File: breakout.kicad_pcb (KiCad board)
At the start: 2 copper layers, 103 x 62 mm, 32 parts, among them CON1 SD_Card, CON2 USB-MICRO-AB, P2 CONN_01X40, P3 CONN_01X40, P4 CONN_01X40, P5 A-DF-09-A/KG-T4S, SW1 SW_PUSH

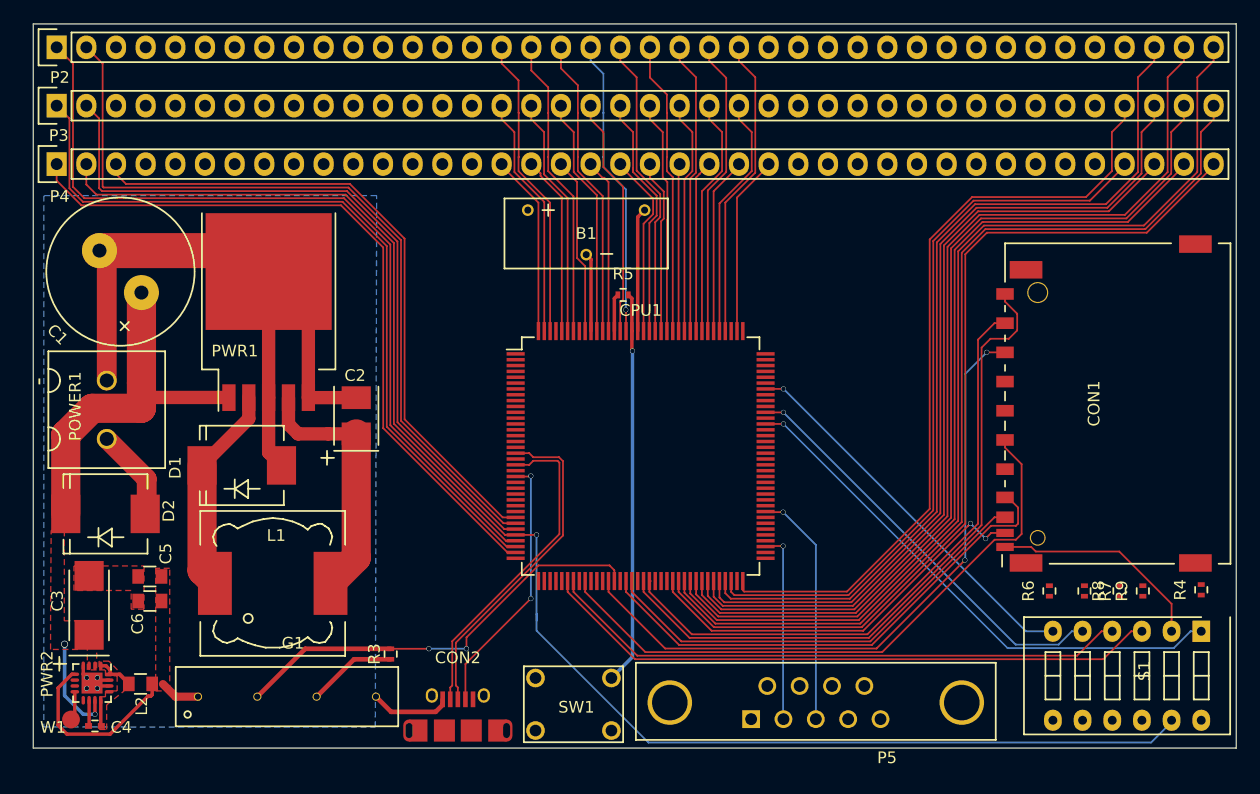
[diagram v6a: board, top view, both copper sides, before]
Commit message: routed right side of IC
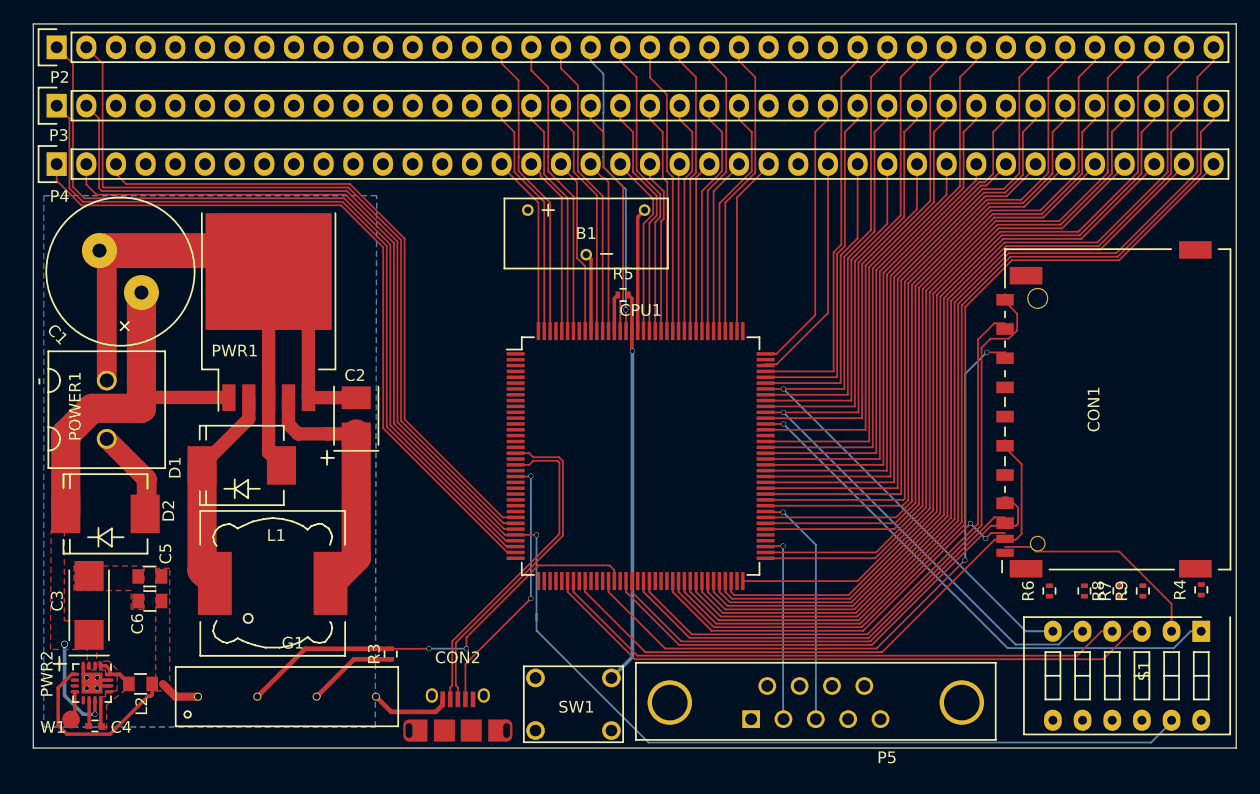
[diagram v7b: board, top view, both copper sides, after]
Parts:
- moved CON1 0.50 mm to (141.2, 146.0)
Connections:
- CPU1 pad 100: (no net) -> /P6_10
- CPU1 pad 101: (no net) -> /P6_11
- CPU1 pad 103: (no net) -> /P6_12
- CPU1 pad 104: (no net) -> /P2_10
- CPU1 pad 105: (no net) -> /P2_11
- CPU1 pad 106: (no net) -> /P2_12
- CPU1 pad 108: (no net) -> /P2_13
- CPU1 pad 73: (no net) -> /P6_0
- CPU1 pad 74: (no net) -> /P6_1
- CPU1 pad 78: (no net) -> /P6_2
- CPU1 pad 79: (no net) -> /P6_3
- CPU1 pad 80: (no net) -> /P6_4
- CPU1 pad 82: (no net) -> /P6_5
- CPU1 pad 83: (no net) -> /P6_6
- CPU1 pad 84: (no net) -> /P2_2
- CPU1 pad 85: (no net) -> /P6_7
- CPU1 pad 86: (no net) -> /P6_8
- CPU1 pad 87: (no net) -> /P2_3
- CPU1 pad 88: (no net) -> /P2_4
- CPU1 pad 89: (no net) -> /USB1_D+
- CPU1 pad 90: (no net) -> /USB1_D-
- CPU1 pad 91: (no net) -> /P2_5
- CPU1 pad 92: (no net) -> /I2C0_SCL
- CPU1 pad 93: (no net) -> /I2C0_SDA
- CPU1 pad 95: (no net) -> /P2_6
- CPU1 pad 97: (no net) -> /P6_9
- CPU1 pad 99: (no net) -> /CLK2
- P2 pad 28: (no net) -> /P2_11
- P2 pad 29: (no net) -> /P2_9
- P2 pad 30: (no net) -> /CLK2
- P2 pad 31: (no net) -> /P2_6
- P2 pad 32: (no net) -> /P2_5
- P2 pad 34: (no net) -> /P6_8
- P2 pad 35: (no net) -> /P6_6
- P2 pad 36: (no net) -> /P6_3
- P2 pad 37: (no net) -> /P6_0
- P3 pad 27: (no net) -> /P2_13
- P3 pad 28: (no net) -> /P2_10
- P3 pad 29: (no net) -> /P6_11
- P3 pad 30: (no net) -> /P2_8
- P3 pad 31: (no net) -> /I2C0_SDA
- P3 pad 32: (no net) -> /USB1_D-
- P3 pad 33: (no net) -> /P2_4
- P3 pad 34: (no net) -> /P6_7
- P3 pad 35: (no net) -> /P6_5
- P3 pad 36: (no net) -> /P6_2
- P4 pad 27: (no net) -> /P2_12
- P4 pad 28: (no net) -> /P6_12
- P4 pad 29: (no net) -> /P6_10
- P4 pad 30: (no net) -> /P6_9
- P4 pad 31: (no net) -> /I2C0_SCL
- P4 pad 32: (no net) -> /USB1_D+
- P4 pad 33: (no net) -> /P2_3
- P4 pad 34: (no net) -> /P2_2
- P4 pad 35: (no net) -> /P6_4
- P4 pad 36: (no net) -> /P6_1
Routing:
- net /P6_0: track 0.00 -> 65.3 mm
- net /P6_3: track 0.00 -> 61.4 mm
- net /P6_6: track 0.00 -> 58.0 mm
- net /P6_2: track 0.00 -> 56.9 mm
- net /P6_8: track 0.00 -> 54.3 mm
- net /P6_5: track 0.00 -> 53.5 mm
- net /P6_1: track 0.00 -> 52.9 mm
- net /P6_7: track 0.00 -> 50.0 mm
- net /P6_4: track 0.00 -> 49.1 mm
- net /P2_5: track 0.00 -> 47.8 mm
- net /P2_4: track 0.00 -> 46.1 mm
- net /P2_2: track 0.00 -> 45.7 mm
- net /P2_6: track 0.00 -> 44.2 mm
- net /USB1_D-: track 0.00 -> 43.5 mm
- net /P2_3: track 0.00 -> 41.8 mm
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
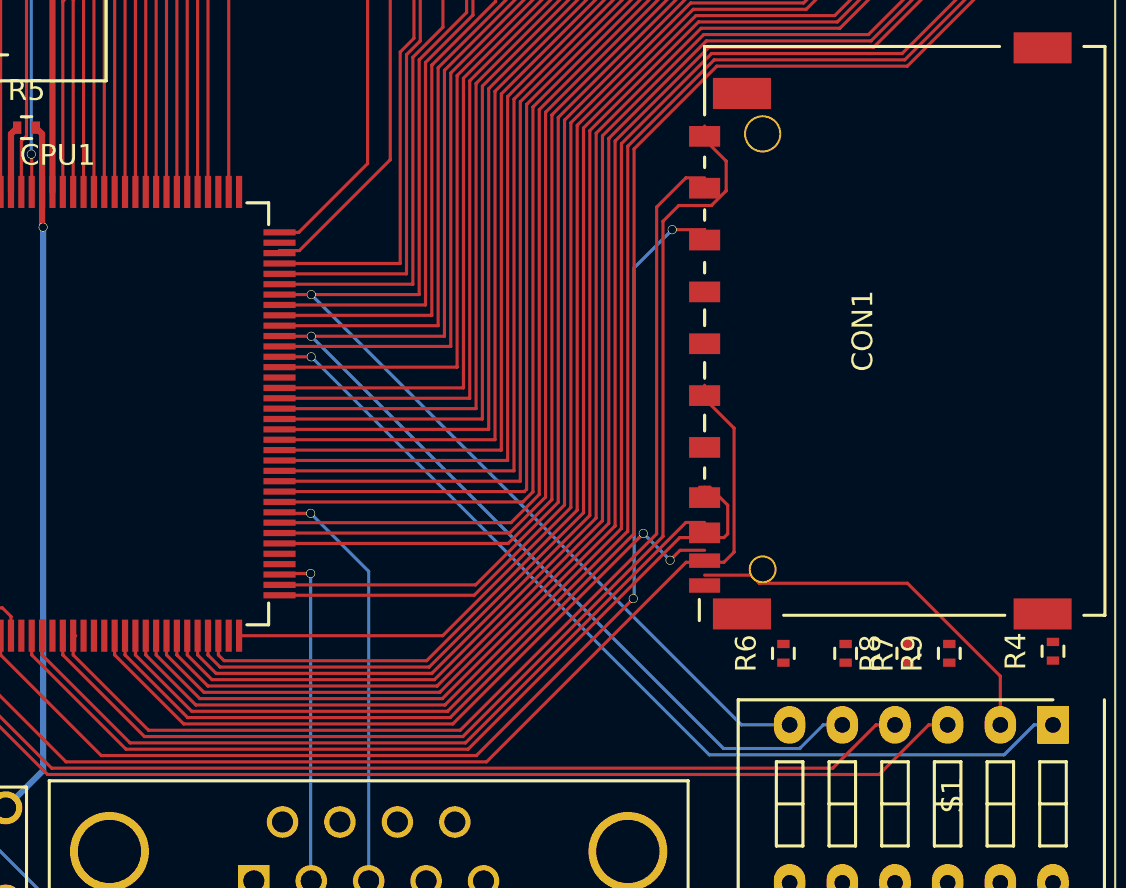
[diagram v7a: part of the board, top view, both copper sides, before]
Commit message: fixed traces to the SD card connector
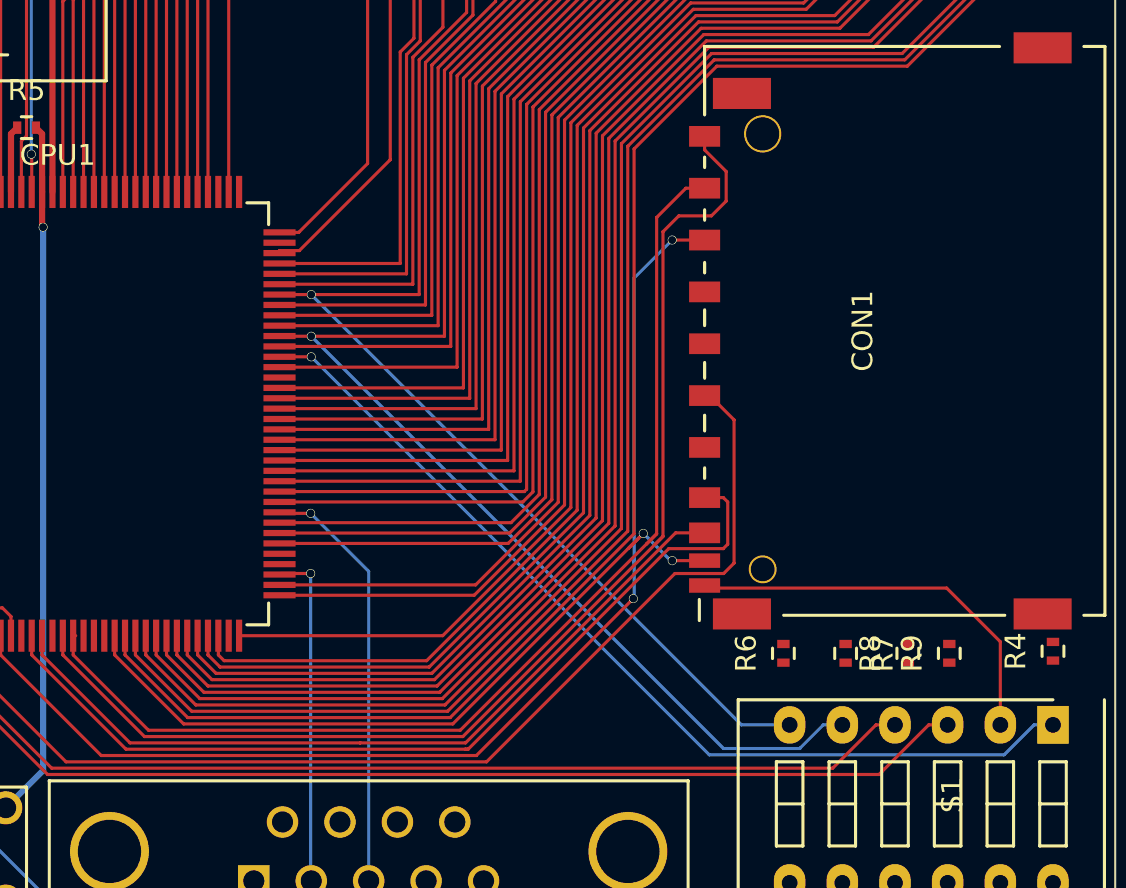
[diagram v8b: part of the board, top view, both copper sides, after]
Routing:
- net /SD_WP: track 18.6 -> 19.4 mm
- net /SD_CD: track 35.3 -> 35.8 mm
